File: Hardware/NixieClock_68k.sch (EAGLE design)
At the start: 72 parts, among them IC1 68008, IC10 7805, IC11 NE555, IC12 74HC08N, IC13 74HC05, IC2 AS6C1008, IC3 39SF020, IC4 DS1244Y, IC5 68681, IC6 74HC30N, IC7 74HC04N, IC8 74HC138N, IC9 74HC266N, Q1 3.6864MHz

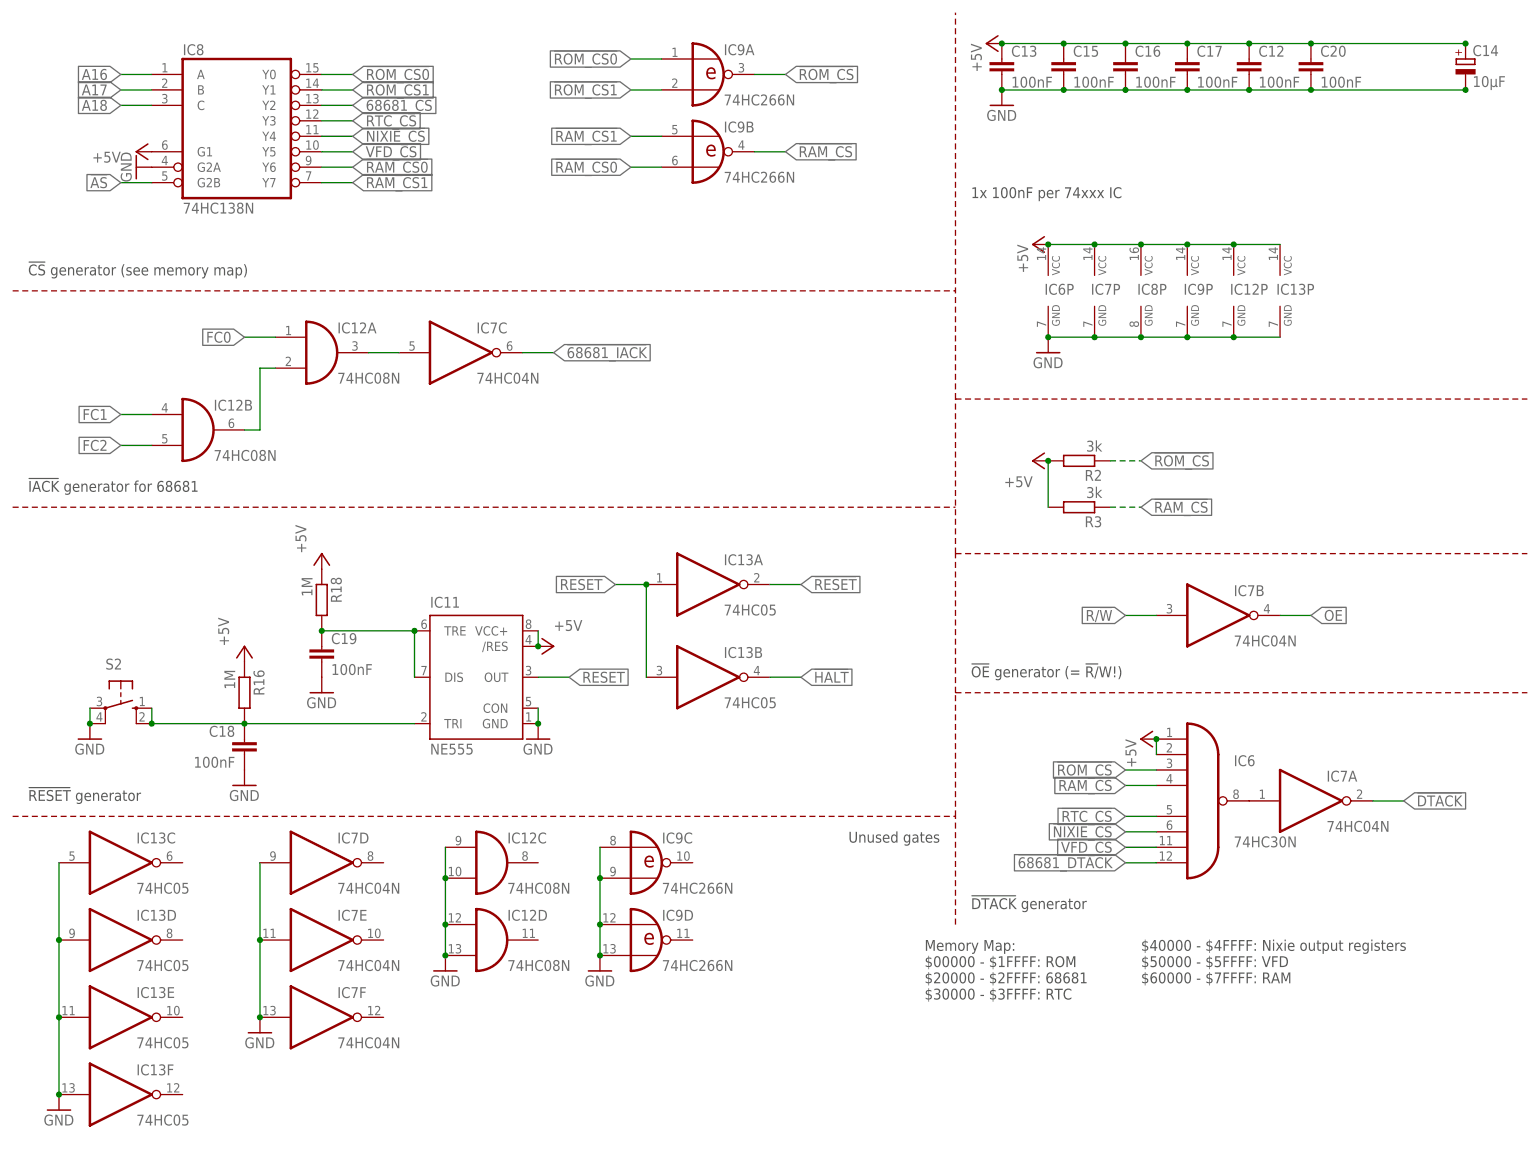
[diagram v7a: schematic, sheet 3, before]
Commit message: updated rom/ram chip select logic
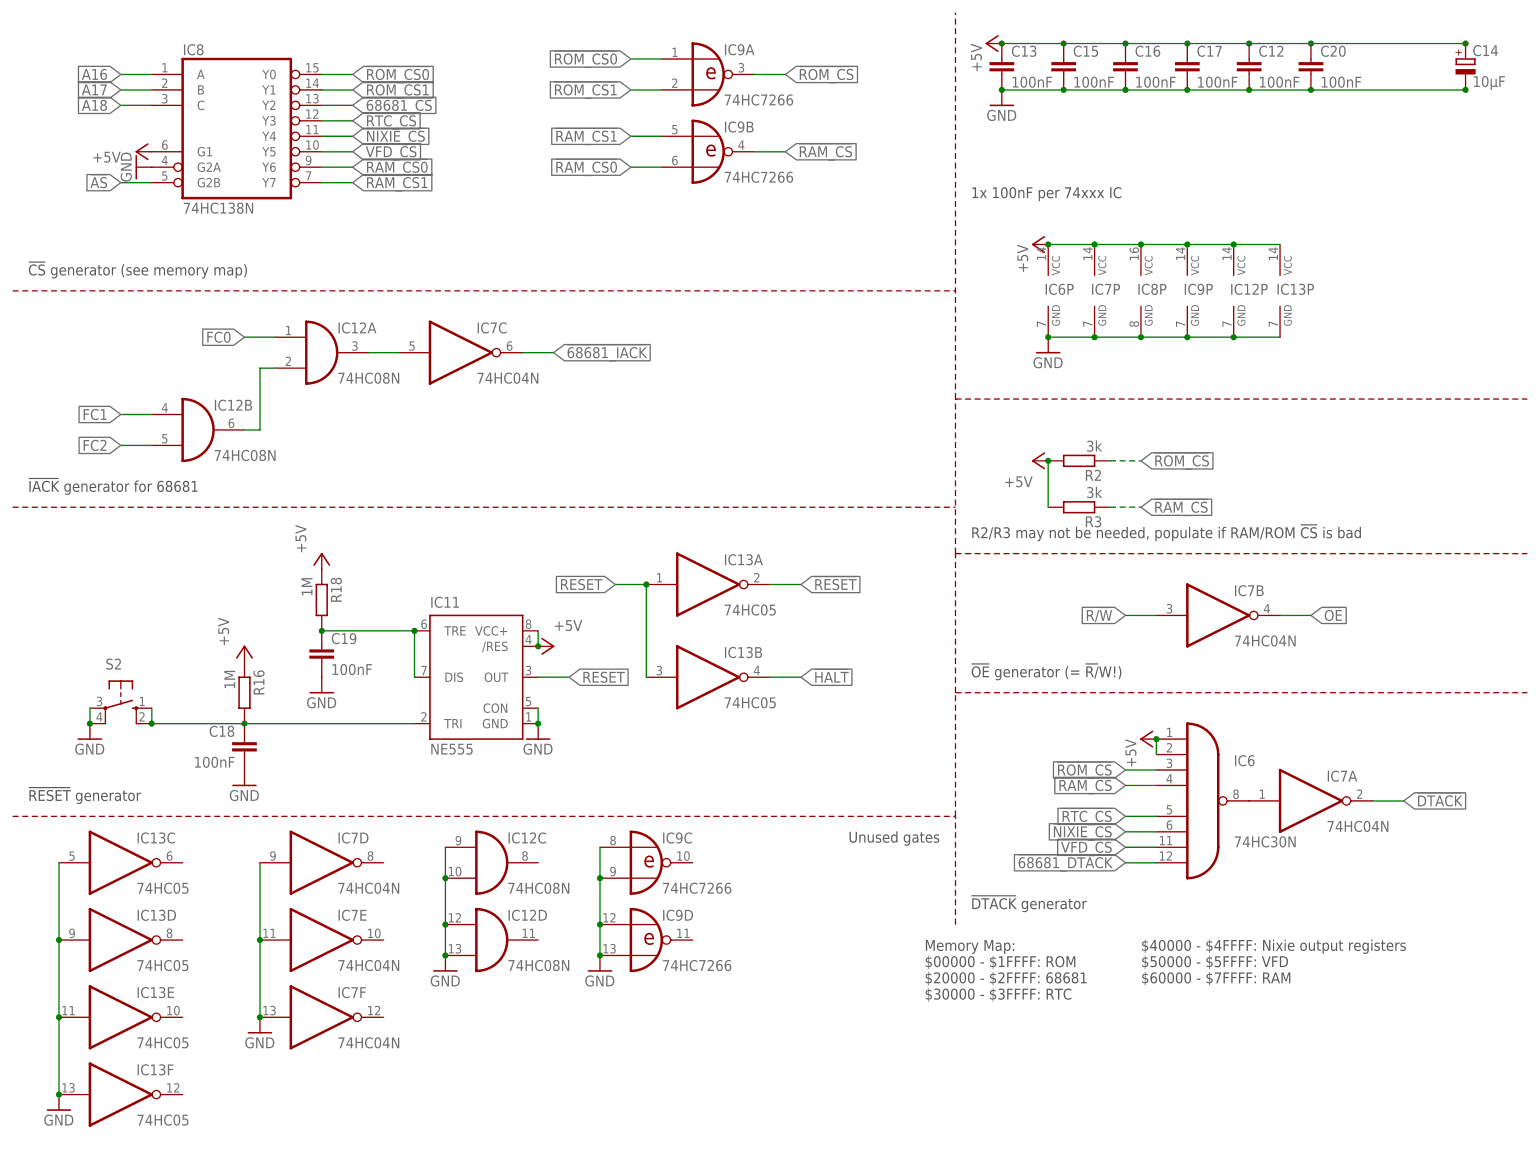
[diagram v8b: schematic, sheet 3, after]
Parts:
- IC9: value 74HC266N -> 74HC7266; MOUSER 595-SN74HC266N -> 595-CD74HC7266E
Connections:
- net OUT0: now also IC5.OP3
- net OUT1: now also IC5.OP1
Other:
- note added: "R2/R3 may not be needed, populate if RAM/ROM !CS! is bad"
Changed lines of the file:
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@@
 <part name="P+17" library="supply1" library_urn="urn:adsk.eagle:library:371" deviceset="+5V" device=""/>
 <part name="GND16" library="supply1" library_urn="urn:adsk.eagle:library:371" deviceset="GND" device=""/>
-<part name="IC9" library="74xx-eu" library_urn="urn:adsk.eagle:library:85" deviceset="74*266" device="N" package3d_urn="urn:adsk.eagle:package:16407/2" technology="HC">
-<attribute name="MOUSER" value="595-SN74HC266N"/>
+<part name="IC9" library="74xx-eu" library_urn="urn:adsk.eagle:library:85" deviceset="74*266" device="N" package3d_urn="urn:adsk.eagle:package:16407/2" technology="HC" value="74HC7266">
+<attribute name="MOUSER" value="595-CD74HC7266E"/>
 </part>
 <part name="IC12" library="74xx-eu" library_urn="urn:adsk.eagle:library:85" deviceset="74*08" device="N" package3d_urn="urn:adsk.eagle:package:16407/2" technology="HC">
@@
 </instances>
 <busses>
-<bus name="!68681_CS,!68681_DTACK,!68681_IACK,68681_X[1..2],A[0..19],D[0..7],!IPL1,!OE,!RTC_CS,R/!W!,STATUS[0..3],UART0_RX,UART1_TX,!VFD_RESET">
+<bus name="!68681_CS,!68681_DTACK,!68681_IACK,A[0..19],CLK,D[0..7],!IPL1,!OE,OUT[0..1],!RESET,!RTC_CS,R/!W!,STATUS[0..1],STATUS[0..3],UART0_RX,UART0_TX,UART1_RX,UART1_TX,!VFD_RESET">
 <segment>
 <wire x1="25.4" y1="177.8" x2="68.58" y2="177.8" width="0.762" layer="92"/>
@@
 <label x="195.58" y="101.6" size="1.778" layer="95" rot="R180" xref="yes"/>
 </segment>
+<segment>
+<pinref part="IC5" gate="G$1" pin="OP3"/>
+<wire x1="60.96" y1="144.78" x2="66.04" y2="144.78" width="0.1524" layer="91"/>
+<wire x1="66.04" y1="144.78" x2="68.58" y2="142.24" width="0.1524" layer="91"/>
+</segment>
 </net>
 <net name="OUT1" class="0">
@@
 <wire x1="215.9" y1="101.6" x2="220.98" y2="101.6" width="0.1524" layer="91"/>
 <label x="220.98" y="101.6" size="1.778" layer="95" xref="yes"/>
+</segment>
+<segment>
+<pinref part="IC5" gate="G$1" pin="OP1"/>
+<wire x1="60.96" y1="149.86" x2="66.04" y2="149.86" width="0.1524" layer="91"/>
+<wire x1="66.04" y1="149.86" x2="68.58" y2="147.32" width="0.1524" layer="91"/>
 </segment>
 </net>
@@
 <text x="2.54" y="55.88" size="1.778" layer="97">!RESET! generator</text>
 <text x="152.4" y="50.8" size="1.778" layer="97" rot="R180">Unused gates</text>
+<text x="157.48" y="99.06" size="1.778" layer="97">R2/R3 may not be needed, populate if RAM/ROM !CS! is bad</text>
 </plain>
 <instances>
